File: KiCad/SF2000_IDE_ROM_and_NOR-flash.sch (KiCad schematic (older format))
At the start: 7 parts, among them J20 Conn_02x11_Odd_Even, U14 SST39LF040, U15 SST39LF802C, U16 74LVC245A

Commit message: Replace 74LVC245A with 74AHCT3G14 for clockport control signals
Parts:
- removed U16: 74LVC245A, Package_SO:TSSOP-20_4.4x6.5mm_P0.65mm, symbol SF2000:74LVC245A
- added U16: 74AHCT3G14, Package_SO:TSSOP-8_3x3mm_P0.65mm, symbol SF2000:74AHCT3G14
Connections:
- no-connect marks 6 -> 2
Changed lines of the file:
@@
 Text GLabel 1450 3250 0    50   Output ~ 0
 IDE_IRQ
-$Comp
-L SF2000:74LVC245A U16
-U 1 1 628D607F
-P 2700 5350
-F 0 "U16" H 2700 5200 50  0000 C CNN
-F 1 "74LVC245A" H 2350 6100 50  0000 C CNN
-F 2 "Package_SO:TSSOP-20_4.4x6.5mm_P0.65mm" H 2700 5350 50  0001 C CNN
-F 3 "http://www.ti.com/lit/gpn/sn74HC245" H 2700 5350 50  0001 C CNN
-	1    2700 5350
-	1    0    0    -1
-$EndComp
-Text GLabel 2700 4550 1    50   Input ~ 0
-3V3
-Text GLabel 2700 6150 3    50   Input ~ 0
-GND
-Text GLabel 2200 5750 0    50   Input ~ 0
-3V3
-Text GLabel 2200 5850 0    50   Input ~ 0
-GND
-Text GLabel 2200 4850 0    50   Input ~ 0
+Text GLabel 4050 4800 0    50   Input ~ 0
 CP_IOWR_FPGA
-Text GLabel 2200 4950 0    50   Input ~ 0
+Text GLabel 4050 5000 0    50   Input ~ 0
 CP_IORD_FPGA
-Text GLabel 2200 5050 0    50   Input ~ 0
+Text GLabel 5050 5000 2    50   Input ~ 0
 CP_CS_FPGA
 Wire Wire Line
@@
 Text GLabel 2950 2950 2    50   Input ~ 0
 CP_IOWR
-Text GLabel 3200 4950 2    50   Output ~ 0
-CP_IORD
-Text GLabel 3200 4850 2    50   Output ~ 0
-CP_IOWR
-Text GLabel 3200 5050 2    50   Output ~ 0
-CP_CS
 Text GLabel 2950 2750 2    50   Input ~ 0
 CP_CS
 Text GLabel 2450 2750 0    50   Output ~ 0
 CP_IRQ
-Text GLabel 2200 5150 0    50   Input ~ 0
+Text GLabel 3050 4050 0    50   Input ~ 0
 CP_IRQ
-Text GLabel 3200 5150 2    50   Output ~ 0
+Text GLabel 3200 4050 2    50   Output ~ 0
 CP_IRQ_FPGA
 Text GLabel 3800 2800 1    50   Input ~ 0
 +5VDC
-Text GLabel 4000 3200 3    50   Input ~ 0
+Text GLabel 4100 3200 3    50   Input ~ 0
 CP_IRQ
 Text GLabel 3900 3200 3    50   Input ~ 0
 CP_RTC_CS
-Text GLabel 4100 3200 3    50   Input ~ 0
+Text GLabel 4000 3200 3    50   Input ~ 0
 CP_RTC_DS
 $Comp
@@
 Wire Wire Line
 	4000 2800 4100 2800
-NoConn ~ 3200 5250
-NoConn ~ 3200 5350
-NoConn ~ 3200 5450
-NoConn ~ 3200 5550
-Text GLabel 2200 5250 0    50   Input ~ 0
+$Comp
+L SF2000:74AHCT3G14 U16
+U 1 1 681A2173
+P 4550 4950
+F 0 "U16" H 4550 5365 50  0000 C CNN
+F 1 "74AHCT3G14" H 4550 5274 50  0000 C CNN
+F 2 "Package_SO:TSSOP-8_3x3mm_P0.65mm" H 4900 5200 50  0001 L CNN
+F 3 "https://assets.nexperia.com/documents/data-sheet/74AHC_AHCT3G14.pdf" H 4900 5100 50  0001 L CNN
+	1    4550 4950
+	1    0    0    -1
+$EndComp
+Text GLabel 5050 4800 2    50   Input ~ 0
++5VDC
+Text GLabel 4050 5100 0    50   Input ~ 0
 GND
-Text GLabel 2200 5350 0    50   Input ~ 0
-GND
-Text GLabel 2200 5450 0    50   Input ~ 0
-GND
-Text GLabel 2200 5550 0    50   Input ~ 0
-GND
+Text GLabel 4050 4900 0    50   Output ~ 0
+CP_CS
+Text GLabel 5050 4900 2    50   Output ~ 0
+CP_IOWR
+Text GLabel 5050 5100 2    50   Output ~ 0
+CP_IORD
 $EndSCHEMATC

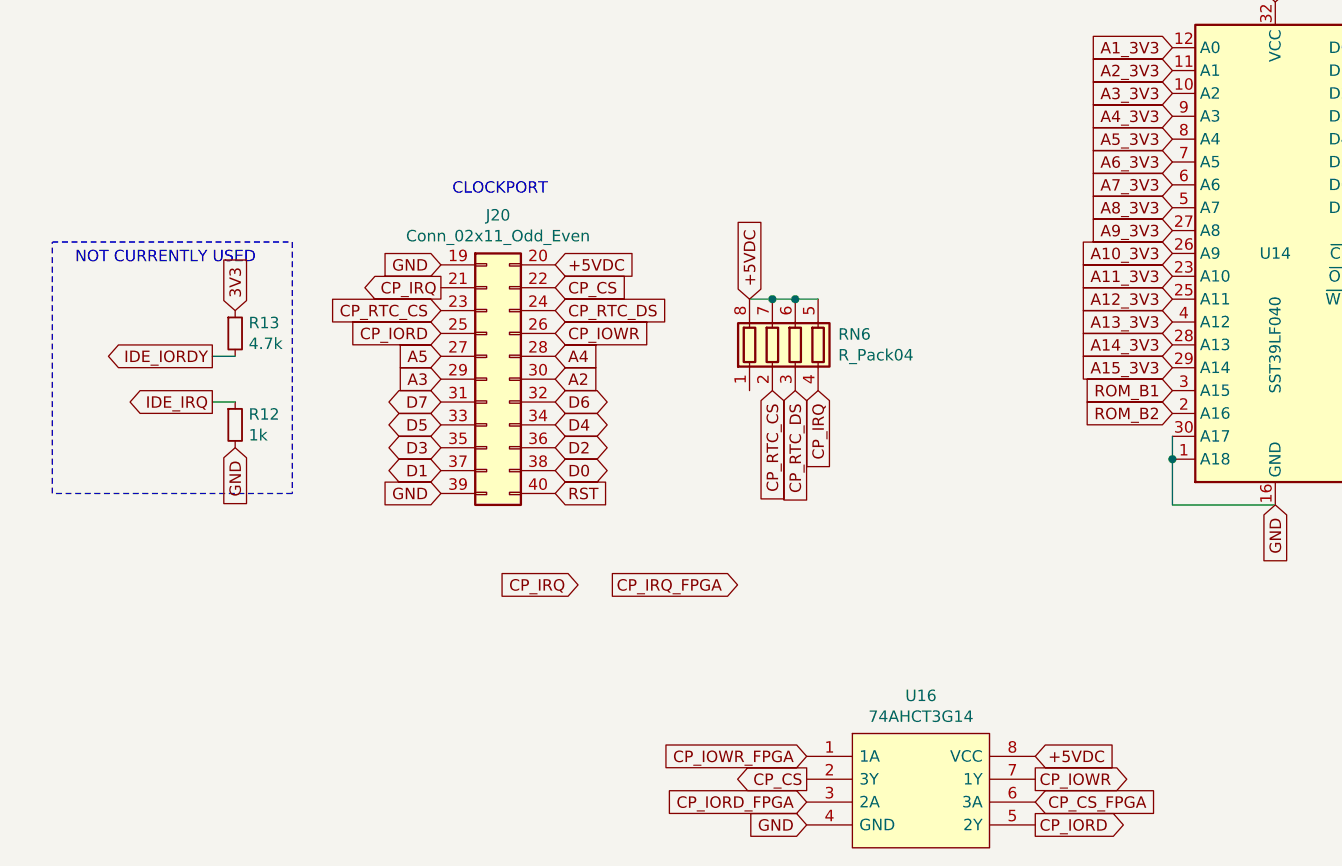
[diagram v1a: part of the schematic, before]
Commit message: Add INT6 signal to clockport
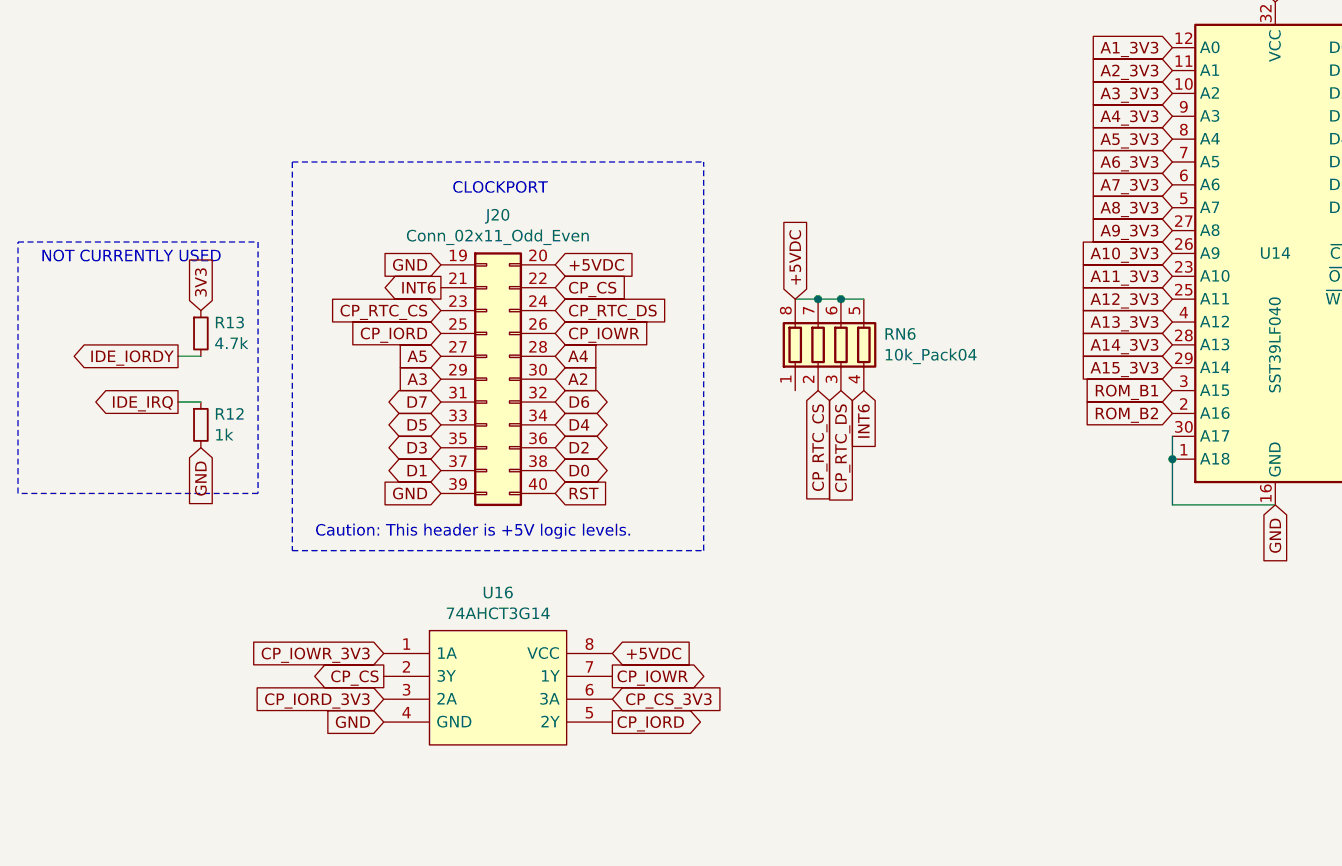
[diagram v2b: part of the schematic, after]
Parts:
- RN6: value R_Pack04 -> 10k_Pack04
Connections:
- net CP_CS_FPGA renamed CP_CS_3V3
- net CP_IORD_FPGA renamed CP_IORD_3V3
- net CP_IOWR_FPGA renamed CP_IOWR_3V3
- net CP_IRQ renamed INT6
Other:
- note added: "Caution: This header is +5V logic levels."
- moved on the sheet: R12, R13, RN6, U16
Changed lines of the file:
@@
 Text GLabel 6550 2400 2    50   BiDi ~ 0
 D7_3V3
-Text GLabel 1450 3050 0    50   Output ~ 0
+Text GLabel 1300 3050 0    50   Output ~ 0
 IDE_IORDY
-Text GLabel 1450 3250 0    50   Output ~ 0
+Text GLabel 1300 3250 0    50   Output ~ 0
 IDE_IRQ
-Text GLabel 4050 4800 0    50   Input ~ 0
-CP_IOWR_FPGA
-Text GLabel 4050 5000 0    50   Input ~ 0
-CP_IORD_FPGA
-Text GLabel 5050 5000 2    50   Input ~ 0
-CP_CS_FPGA
+Text GLabel 2200 4350 0    50   Input ~ 0
+CP_IOWR_3V3
+Text GLabel 2200 4550 0    50   Input ~ 0
+CP_IORD_3V3
+Text GLabel 3200 4550 2    50   Input ~ 0
+CP_CS_3V3
 Wire Wire Line
 	6100 3700 5650 3700
@@
 L Device:R_Small R?
 U 1 1 62340B55
-P 1550 2950
+P 1400 2950
 AR Path="/62340B55" Ref="R?"  Part="1"
 AR Path="/620D263D/62340B55" Ref="R?"  Part="1"
 AR Path="/627A6500/62340B55" Ref="R13"  Part="1"
-F 0 "R13" H 1609 2996 50  0000 L CNN
-F 1 "4.7k" H 1609 2905 50  0000 L CNN
-F 2 "Resistor_SMD:R_0805_2012Metric_Pad1.15x1.40mm_HandSolder" H 1550 2950 50  0001 C CNN
-F 3 "~" H 1550 2950 50  0001 C CNN
-	1    1550 2950
+F 0 "R13" H 1459 2996 50  0000 L CNN
+F 1 "4.7k" H 1459 2905 50  0000 L CNN
+F 2 "Resistor_SMD:R_0805_2012Metric_Pad1.15x1.40mm_HandSolder" H 1400 2950 50  0001 C CNN
+F 3 "~" H 1400 2950 50  0001 C CNN
+	1    1400 2950
 	1    0    0    -1
 $EndComp
@@
 L Device:R_Small R?
 U 1 1 62340D58
-P 1550 3350
+P 1400 3350
 AR Path="/62340D58" Ref="R?"  Part="1"
 AR Path="/620D263D/62340D58" Ref="R?"  Part="1"
 AR Path="/627A6500/62340D58" Ref="R12"  Part="1"
-F 0 "R12" H 1609 3396 50  0000 L CNN
-F 1 "1k" H 1609 3305 50  0000 L CNN
-F 2 "Resistor_SMD:R_0805_2012Metric_Pad1.15x1.40mm_HandSolder" H 1550 3350 50  0001 C CNN
-F 3 "~" H 1550 3350 50  0001 C CNN
-	1    1550 3350
+F 0 "R12" H 1459 3396 50  0000 L CNN
+F 1 "1k" H 1459 3305 50  0000 L CNN
+F 2 "Resistor_SMD:R_0805_2012Metric_Pad1.15x1.40mm_HandSolder" H 1400 3350 50  0001 C CNN
+F 3 "~" H 1400 3350 50  0001 C CNN
+	1    1400 3350
 	1    0    0    -1
 $EndComp
-Text GLabel 1550 3450 3    50   Input ~ 0
+Text GLabel 1400 3450 3    50   Input ~ 0
 GND
 Wire Wire Line
-	1550 3250 1450 3250
+	1400 3250 1300 3250
 Wire Wire Line
-	1550 3050 1450 3050
-Text GLabel 1550 2850 1    50   Input ~ 0
+	1400 3050 1300 3050
+Text GLabel 1400 2850 1    50   Input ~ 0
 3V3
 Wire Notes Line
-	750  2550 1800 2550
+	600  2550 1650 2550
 Wire Notes Line
-	1800 2550 1800 3650
+	1650 2550 1650 3650
 Wire Notes Line
-	1800 3650 750  3650
+	1650 3650 600  3650
 Wire Notes Line
-	750  3650 750  2550
-Text Notes 850  2650 0    50   ~ 0
+	600  3650 600  2550
+Text Notes 700  2650 0    50   ~ 0
 NOT CURRENTLY USED
 NoConn ~ 8550 3000
@@
 Text GLabel 2950 2750 2    50   Input ~ 0
 CP_CS
-Text GLabel 2450 2750 0    50   Output ~ 0
-CP_IRQ
-Text GLabel 3050 4050 0    50   Input ~ 0
-CP_IRQ
-Text GLabel 3200 4050 2    50   Output ~ 0
-CP_IRQ_FPGA
-Text GLabel 3800 2800 1    50   Input ~ 0
+Text GLabel 4000 2800 1    50   Input ~ 0
 +5VDC
+Text GLabel 4300 3200 3    50   Input ~ 0
+INT6
 Text GLabel 4100 3200 3    50   Input ~ 0
-CP_IRQ
-Text GLabel 3900 3200 3    50   Input ~ 0
 CP_RTC_CS
-Text GLabel 4000 3200 3    50   Input ~ 0
+Text GLabel 4200 3200 3    50   Input ~ 0
 CP_RTC_DS
 $Comp
 L Device:R_Pack04 RN6
 U 1 1 680E7107
-P 4000 3000
-F 0 "RN6" H 4188 3046 50  0000 L CNN
-F 1 "R_Pack04" H 4188 2955 50  0000 L CNN
-F 2 "SF2000:RESCAF80P320X160X60-8N" V 4275 3000 50  0001 C CNN
-F 3 "~" H 4000 3000 50  0001 C CNN
-	1    4000 3000
+P 4200 3000
+F 0 "RN6" H 4388 3046 50  0000 L CNN
+F 1 "10k_Pack04" H 4388 2955 50  0000 L CNN
+F 2 "SF2000:RESCAF80P320X160X60-8N" V 4475 3000 50  0001 C CNN
+F 3 "~" H 4200 3000 50  0001 C CNN
+	1    4200 3000
 	1    0    0    -1
 $EndComp
 Wire Wire Line
-	3800 2800 3900 2800
+	4000 2800 4100 2800
 Wire Wire Line
-	3900 2800 4000 2800
-Connection ~ 3900 2800
-Connection ~ 4000 2800
+	4100 2800 4200 2800
+Connection ~ 4100 2800
+Connection ~ 4200 2800
 Wire Wire Line
-	4000 2800 4100 2800
+	4200 2800 4300 2800
 $Comp
 L SF2000:74AHCT3G14 U16
 U 1 1 681A2173
-P 4550 4950
-F 0 "U16" H 4550 5365 50  0000 C CNN
-F 1 "74AHCT3G14" H 4550 5274 50  0000 C CNN
-F 2 "Package_SO:TSSOP-8_3x3mm_P0.65mm" H 4900 5200 50  0001 L CNN
-F 3 "https://assets.nexperia.com/documents/data-sheet/74AHC_AHCT3G14.pdf" H 4900 5100 50  0001 L CNN
-	1    4550 4950
+P 2700 4500
+F 0 "U16" H 2700 4915 50  0000 C CNN
+F 1 "74AHCT3G14" H 2700 4824 50  0000 C CNN
+F 2 "Package_SO:TSSOP-8_3x3mm_P0.65mm" H 3050 4750 50  0001 L CNN
+F 3 "https://assets.nexperia.com/documents/data-sheet/74AHC_AHCT3G14.pdf" H 3050 4650 50  0001 L CNN
+	1    2700 4500
 	1    0    0    -1
 $EndComp
-Text GLabel 5050 4800 2    50   Input ~ 0
+Text GLabel 3200 4350 2    50   Input ~ 0
 +5VDC
-Text GLabel 4050 5100 0    50   Input ~ 0
+Text GLabel 2200 4650 0    50   Input ~ 0
 GND
-Text GLabel 4050 4900 0    50   Output ~ 0
+Text GLabel 2200 4450 0    50   Output ~ 0
 CP_CS
-Text GLabel 5050 4900 2    50   Output ~ 0
+Text GLabel 3200 4450 2    50   Output ~ 0
 CP_IOWR
-Text GLabel 5050 5100 2    50   Output ~ 0
+Text GLabel 3200 4650 2    50   Output ~ 0
 CP_IORD
+Text GLabel 2450 2750 0    50   Output ~ 0
+INT6
+Text Notes 1900 3850 0    50   ~ 0
+Caution: This header is +5V logic levels.
+Wire Notes Line
+	1800 2200 1800 3900
+Wire Notes Line
+	1800 3900 3600 3900
+Wire Notes Line
+	3600 3900 3600 2200
+Wire Notes Line
+	1800 2200 3600 2200
 $EndSCHEMATC

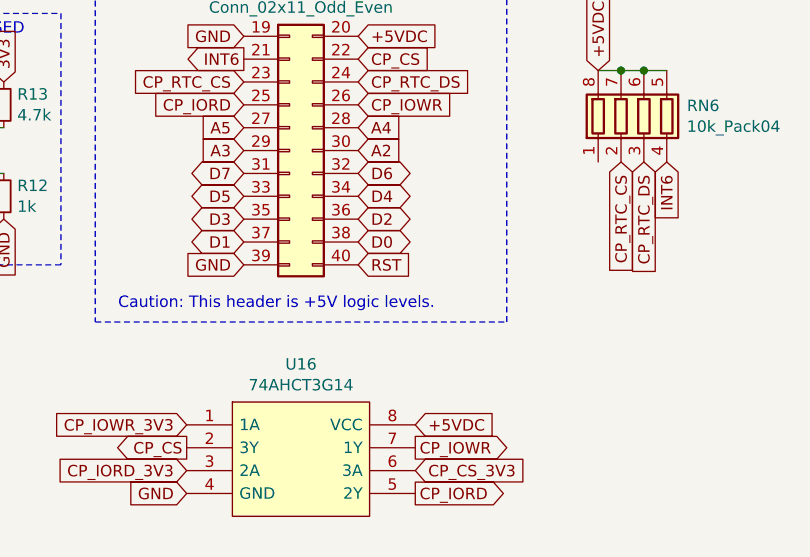
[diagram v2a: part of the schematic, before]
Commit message: Add SD_LED & LED Activity circuit and small fixes and routing around the clockport area
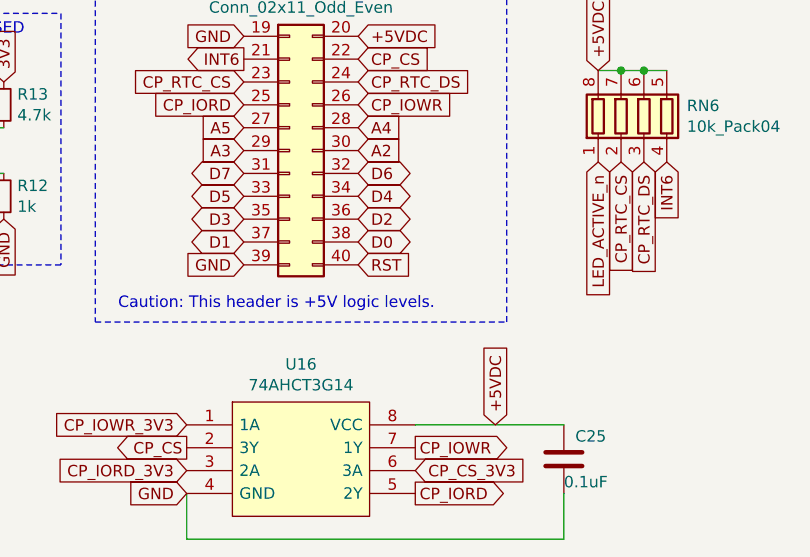
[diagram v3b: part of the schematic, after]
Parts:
- added C25: 0.1uF, Capacitor_SMD:C_0805_2012Metric_Pad1.18x1.45mm_HandSolder, symbol Device:C
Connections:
- net +5VDC: now also C25.1
- net GND: now also C25.2
- net LED_ACTIVE_n: now reaches RN6.1 (R1.1)
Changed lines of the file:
@@
 	1    0    0    -1
 $EndComp
-Text GLabel 3200 4350 2    50   Input ~ 0
+Text GLabel 3550 4350 1    50   Input ~ 0
 +5VDC
 Text GLabel 2200 4650 0    50   Input ~ 0
@@
 Wire Notes Line
 	1800 2200 3600 2200
+Text GLabel 4000 3200 3    50   Input ~ 0
+LED_ACTIVE_n
+$Comp
+L Device:C C?
+U 1 1 683D3421
+P 3850 4500
+AR Path="/683D3421" Ref="C?"  Part="1"
+AR Path="/620D263D/683D3421" Ref="C?"  Part="1"
+AR Path="/627A6500/683D3421" Ref="C25"  Part="1"
+F 0 "C25" H 3900 4600 50  0000 L CNN
+F 1 "0.1uF" H 3850 4400 50  0000 L CNN
+F 2 "Capacitor_SMD:C_0805_2012Metric_Pad1.18x1.45mm_HandSolder" H 3888 4350 50  0001 C CNN
+F 3 "~" H 3850 4500 50  0001 C CNN
+	1    3850 4500
+	1    0    0    -1
+$EndComp
+Wire Wire Line
+	3850 4350 3200 4350
+Wire Wire Line
+	3850 4650 3850 4850
+Wire Wire Line
+	3850 4850 2200 4850
+Wire Wire Line
+	2200 4850 2200 4650
 $EndSCHEMATC

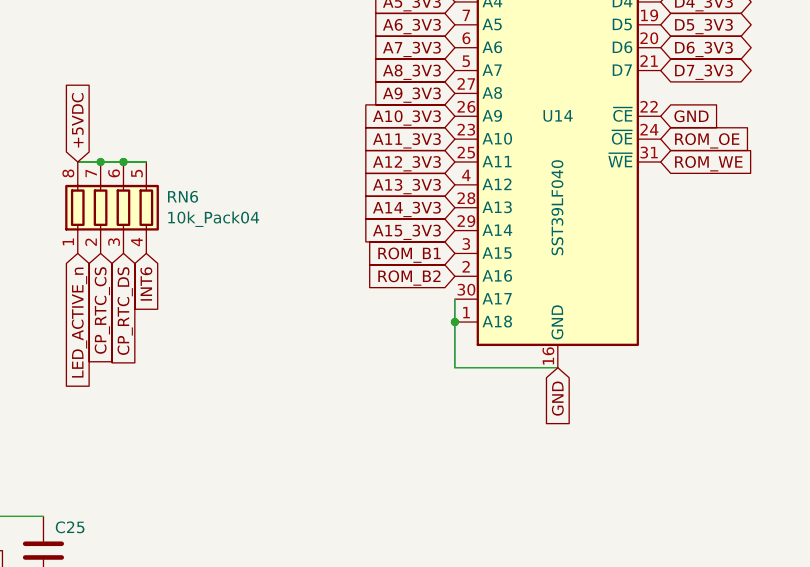
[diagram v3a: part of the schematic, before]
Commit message: Fixed driver bank select jumper for ROM at U14, pulled-up by vacant resistor in RN3
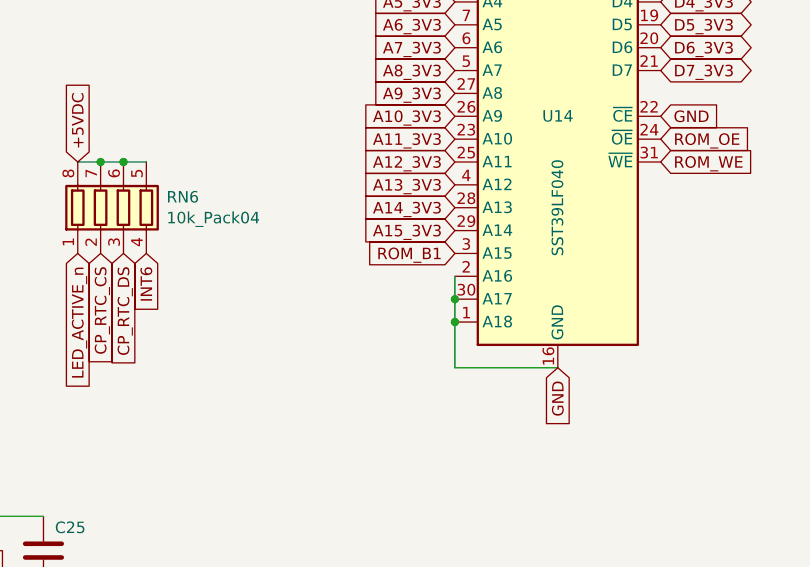
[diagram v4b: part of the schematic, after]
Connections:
- net ROM_B2 is gone; now on net GND: U14.2 (A16)
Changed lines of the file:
@@
 Text GLabel 5650 3200 0    50   Input ~ 0
 ROM_B1
-Text GLabel 5650 3300 0    50   Input ~ 0
-ROM_B2
 Text GLabel 9550 3500 2    50   BiDi ~ 0
 D0_3V3
@@
 Wire Wire Line
 	2200 4850 2200 4650
+Wire Wire Line
+	5650 3300 5650 3400
+Connection ~ 5650 3400
 $EndSCHEMATC

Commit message: Remove R12,R13
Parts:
- removed R12: 1k, Resistor_SMD:R_0805_2012Metric_Pad1.15x1.40mm_HandSolder, symbol Device:R_Small
- removed R13: 4.7k, Resistor_SMD:R_0805_2012Metric_Pad1.15x1.40mm_HandSolder, symbol Device:R_Small
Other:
- note removed: "NOT CURRENTLY USED"
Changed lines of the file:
@@
 Text GLabel 6550 2400 2    50   BiDi ~ 0
 D7_3V3
-Text GLabel 1300 3050 0    50   Output ~ 0
-IDE_IORDY
-Text GLabel 1300 3250 0    50   Output ~ 0
-IDE_IRQ
 Text GLabel 2200 4350 0    50   Input ~ 0
 CP_IOWR_3V3
@@
 Text GLabel 6100 1500 1    50   Input ~ 0
 3V3
-$Comp
-L Device:R_Small R?
-U 1 1 62340B55
-P 1400 2950
-AR Path="/62340B55" Ref="R?"  Part="1"
-AR Path="/620D263D/62340B55" Ref="R?"  Part="1"
-AR Path="/627A6500/62340B55" Ref="R13"  Part="1"
-F 0 "R13" H 1459 2996 50  0000 L CNN
-F 1 "4.7k" H 1459 2905 50  0000 L CNN
-F 2 "Resistor_SMD:R_0805_2012Metric_Pad1.15x1.40mm_HandSolder" H 1400 2950 50  0001 C CNN
-F 3 "~" H 1400 2950 50  0001 C CNN
-	1    1400 2950
-	1    0    0    -1
-$EndComp
-$Comp
-L Device:R_Small R?
-U 1 1 62340D58
-P 1400 3350
-AR Path="/62340D58" Ref="R?"  Part="1"
-AR Path="/620D263D/62340D58" Ref="R?"  Part="1"
-AR Path="/627A6500/62340D58" Ref="R12"  Part="1"
-F 0 "R12" H 1459 3396 50  0000 L CNN
-F 1 "1k" H 1459 3305 50  0000 L CNN
-F 2 "Resistor_SMD:R_0805_2012Metric_Pad1.15x1.40mm_HandSolder" H 1400 3350 50  0001 C CNN
-F 3 "~" H 1400 3350 50  0001 C CNN
-	1    1400 3350
-	1    0    0    -1
-$EndComp
-Text GLabel 1400 3450 3    50   Input ~ 0
-GND
-Wire Wire Line
-	1400 3250 1300 3250
-Wire Wire Line
-	1400 3050 1300 3050
-Text GLabel 1400 2850 1    50   Input ~ 0
-3V3
-Wire Notes Line
-	600  2550 1650 2550
-Wire Notes Line
-	1650 2550 1650 3650
-Wire Notes Line
-	1650 3650 600  3650
-Wire Notes Line
-	600  3650 600  2550
-Text Notes 700  2650 0    50   ~ 0
-NOT CURRENTLY USED
 NoConn ~ 8550 3000
 NoConn ~ 8550 2900
